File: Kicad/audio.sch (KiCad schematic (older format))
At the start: 71 parts, among them J601 Line Out, J602 AC'97 Audio Header, J603 CD Audio In, U601 TLV320AIC23BPW, U602 STX-4335-5BGP-S1, Y601 12M

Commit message: Switch some of the radial THT Electrolytic caps for SMD MLCCs.
Also changed the STM32 for an LQFP-32 as it has a bigger pitch on the
pins.

The LQFP is easier to solder than the TSSOP, and the MLCC takes are
cheaper and take up less space.
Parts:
- C601, C603, C611, C626, C633, C634, C635, C636, C637, C638: value 10u -> 10u 10V; footprint Capacitor_THT:CP_Radial_D6.3mm_P2.50mm -> Capacitor_SMD:C_0805_2012Metric_Pad1.15x1.40mm_HandSolder; symbol Device:CP -> Device:C; Digikey 493-10359-1-ND -> 1276-6455-1-ND; MPN UMW1E100MDD1TP -> CL21A106KOQNNNG; Manufacturer Nichicon -> Samsung
- C605, C606, C620, C621: symbol Device:CP_Small -> Device:C_Small
- C614, C615: value 220u -> 220u 16V
- C630: value 1u -> 1u 10V; footprint Capacitor_THT:CP_Radial_D6.3mm_P2.50mm -> Capacitor_SMD:C_0805_2012Metric_Pad1.15x1.40mm_HandSolder; symbol Device:CP_Small -> Device:C_Small; Digikey 493-10944-1-ND -> 1276-6471-1-ND; MPN UFG1H010MDM1TD -> CL21B105KOFNNNG; Manufacturer Nichicon -> Samsung
- FB601, FB602, FB603, FB604, FB605, FB606, FB608, FB609, FB610, FB611: value 220R@100MHz -> 3k3
- R601, R602: value 100 -> 100R
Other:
- moved on the sheet: C602, C607, C609, C610, C612, C613, C627, FB601, FB611

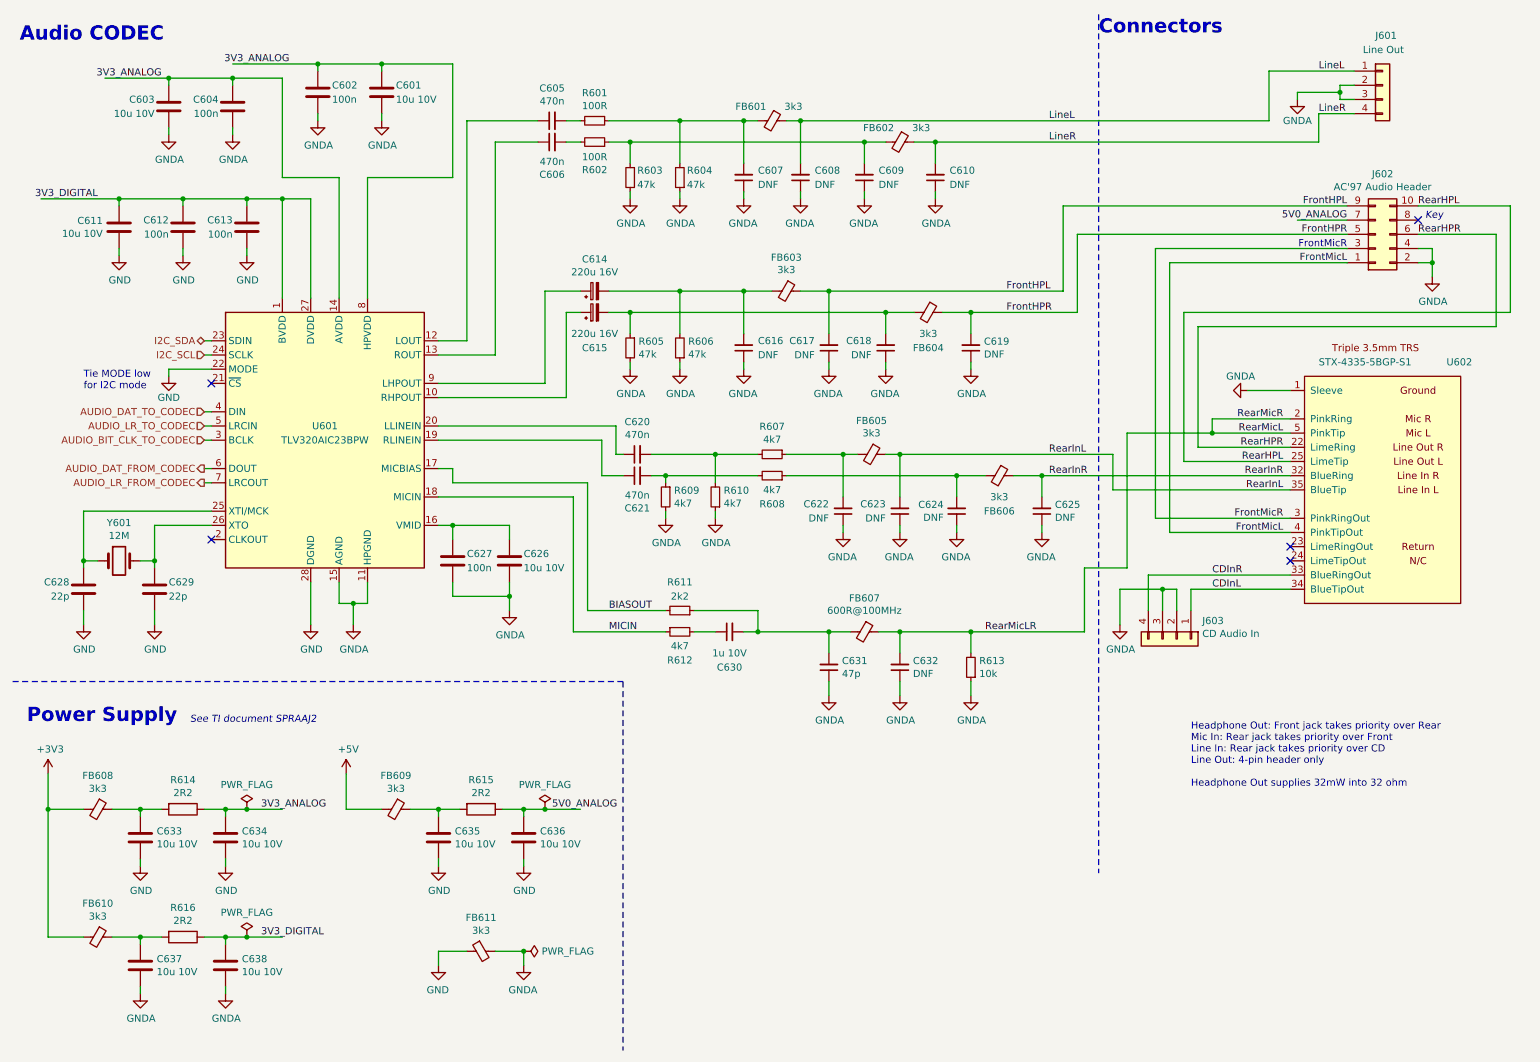
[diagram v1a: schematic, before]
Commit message: Added 12-bit video DAC.
Also had to change footprints to suit Kicad 5.1.9
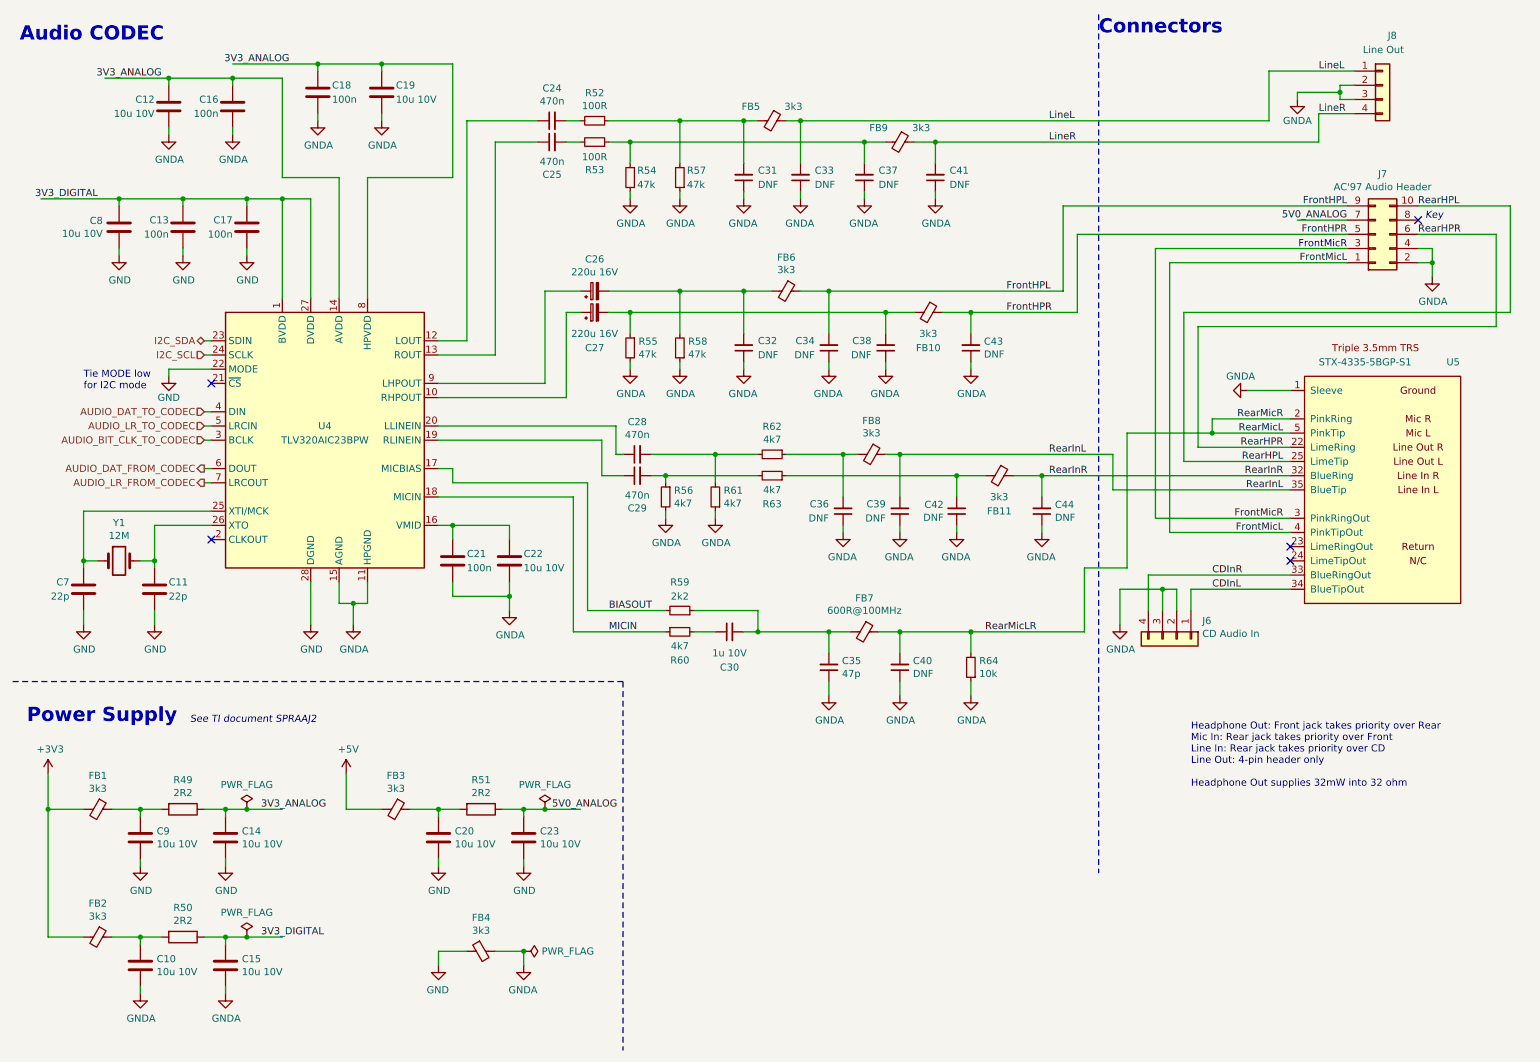
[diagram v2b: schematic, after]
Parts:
- C10: renamed from C637; footprint Capacitor_SMD:C_0805_2012Metric_Pad1.15x1.40mm_HandSolder -> Capacitor_SMD:C_0805_2012Metric_Pad1.18x1.45mm_HandSolder
- C11: renamed from C629; footprint Capacitor_SMD:C_0805_2012Metric_Pad1.15x1.40mm_HandSolder -> Capacitor_SMD:C_0805_2012Metric_Pad1.18x1.45mm_HandSolder
- C12: renamed from C603; footprint Capacitor_SMD:C_0805_2012Metric_Pad1.15x1.40mm_HandSolder -> Capacitor_SMD:C_0805_2012Metric_Pad1.18x1.45mm_HandSolder
- C13: renamed from C612; footprint Capacitor_SMD:C_0805_2012Metric_Pad1.15x1.40mm_HandSolder -> Capacitor_SMD:C_0805_2012Metric_Pad1.18x1.45mm_HandSolder
- C14: renamed from C634; footprint Capacitor_SMD:C_0805_2012Metric_Pad1.15x1.40mm_HandSolder -> Capacitor_SMD:C_0805_2012Metric_Pad1.18x1.45mm_HandSolder
- C15: renamed from C638; footprint Capacitor_SMD:C_0805_2012Metric_Pad1.15x1.40mm_HandSolder -> Capacitor_SMD:C_0805_2012Metric_Pad1.18x1.45mm_HandSolder
- C16: renamed from C604; footprint Capacitor_SMD:C_0805_2012Metric_Pad1.15x1.40mm_HandSolder -> Capacitor_SMD:C_0805_2012Metric_Pad1.18x1.45mm_HandSolder
- C17: renamed from C613; footprint Capacitor_SMD:C_0805_2012Metric_Pad1.15x1.40mm_HandSolder -> Capacitor_SMD:C_0805_2012Metric_Pad1.18x1.45mm_HandSolder
- C18: renamed from C602; footprint Capacitor_SMD:C_0805_2012Metric_Pad1.15x1.40mm_HandSolder -> Capacitor_SMD:C_0805_2012Metric_Pad1.18x1.45mm_HandSolder
- C19: renamed from C601; footprint Capacitor_SMD:C_0805_2012Metric_Pad1.15x1.40mm_HandSolder -> Capacitor_SMD:C_0805_2012Metric_Pad1.18x1.45mm_HandSolder
- C20: renamed from C635; footprint Capacitor_SMD:C_0805_2012Metric_Pad1.15x1.40mm_HandSolder -> Capacitor_SMD:C_0805_2012Metric_Pad1.18x1.45mm_HandSolder
- C21: renamed from C627; footprint Capacitor_SMD:C_0805_2012Metric_Pad1.15x1.40mm_HandSolder -> Capacitor_SMD:C_0805_2012Metric_Pad1.18x1.45mm_HandSolder
- C22: renamed from C626; footprint Capacitor_SMD:C_0805_2012Metric_Pad1.15x1.40mm_HandSolder -> Capacitor_SMD:C_0805_2012Metric_Pad1.18x1.45mm_HandSolder
- C23: renamed from C636; footprint Capacitor_SMD:C_0805_2012Metric_Pad1.15x1.40mm_HandSolder -> Capacitor_SMD:C_0805_2012Metric_Pad1.18x1.45mm_HandSolder
- C24: renamed from C605; footprint Capacitor_SMD:C_0805_2012Metric_Pad1.15x1.40mm_HandSolder -> Capacitor_SMD:C_0805_2012Metric_Pad1.18x1.45mm_HandSolder
- C25: renamed from C606; footprint Capacitor_SMD:C_0805_2012Metric_Pad1.15x1.40mm_HandSolder -> Capacitor_SMD:C_0805_2012Metric_Pad1.18x1.45mm_HandSolder
- C28: renamed from C620; footprint Capacitor_SMD:C_0805_2012Metric_Pad1.15x1.40mm_HandSolder -> Capacitor_SMD:C_0805_2012Metric_Pad1.18x1.45mm_HandSolder
- C29: renamed from C621; footprint Capacitor_SMD:C_0805_2012Metric_Pad1.15x1.40mm_HandSolder -> Capacitor_SMD:C_0805_2012Metric_Pad1.18x1.45mm_HandSolder
- C30: renamed from C630; footprint Capacitor_SMD:C_0805_2012Metric_Pad1.15x1.40mm_HandSolder -> Capacitor_SMD:C_0805_2012Metric_Pad1.18x1.45mm_HandSolder
- C31: renamed from C607; footprint Capacitor_SMD:C_0805_2012Metric_Pad1.15x1.40mm_HandSolder -> Capacitor_SMD:C_0805_2012Metric_Pad1.18x1.45mm_HandSolder
- C32: renamed from C616; footprint Capacitor_SMD:C_0805_2012Metric_Pad1.15x1.40mm_HandSolder -> Capacitor_SMD:C_0805_2012Metric_Pad1.18x1.45mm_HandSolder
- C33: renamed from C608; footprint Capacitor_SMD:C_0805_2012Metric_Pad1.15x1.40mm_HandSolder -> Capacitor_SMD:C_0805_2012Metric_Pad1.18x1.45mm_HandSolder
- C34: renamed from C617; footprint Capacitor_SMD:C_0805_2012Metric_Pad1.15x1.40mm_HandSolder -> Capacitor_SMD:C_0805_2012Metric_Pad1.18x1.45mm_HandSolder
- C35: renamed from C631; footprint Capacitor_SMD:C_0805_2012Metric_Pad1.15x1.40mm_HandSolder -> Capacitor_SMD:C_0805_2012Metric_Pad1.18x1.45mm_HandSolder
- C36: renamed from C622; footprint Capacitor_SMD:C_0805_2012Metric_Pad1.15x1.40mm_HandSolder -> Capacitor_SMD:C_0805_2012Metric_Pad1.18x1.45mm_HandSolder
- C37: renamed from C609; footprint Capacitor_SMD:C_0805_2012Metric_Pad1.15x1.40mm_HandSolder -> Capacitor_SMD:C_0805_2012Metric_Pad1.18x1.45mm_HandSolder
- C38: renamed from C618; footprint Capacitor_SMD:C_0805_2012Metric_Pad1.15x1.40mm_HandSolder -> Capacitor_SMD:C_0805_2012Metric_Pad1.18x1.45mm_HandSolder
- C39: renamed from C623; footprint Capacitor_SMD:C_0805_2012Metric_Pad1.15x1.40mm_HandSolder -> Capacitor_SMD:C_0805_2012Metric_Pad1.18x1.45mm_HandSolder
- C40: renamed from C632; footprint Capacitor_SMD:C_0805_2012Metric_Pad1.15x1.40mm_HandSolder -> Capacitor_SMD:C_0805_2012Metric_Pad1.18x1.45mm_HandSolder
- C41: renamed from C610; footprint Capacitor_SMD:C_0805_2012Metric_Pad1.15x1.40mm_HandSolder -> Capacitor_SMD:C_0805_2012Metric_Pad1.18x1.45mm_HandSolder
- C42: renamed from C624; footprint Capacitor_SMD:C_0805_2012Metric_Pad1.15x1.40mm_HandSolder -> Capacitor_SMD:C_0805_2012Metric_Pad1.18x1.45mm_HandSolder
- C43: renamed from C619; footprint Capacitor_SMD:C_0805_2012Metric_Pad1.15x1.40mm_HandSolder -> Capacitor_SMD:C_0805_2012Metric_Pad1.18x1.45mm_HandSolder
- C44: renamed from C625; footprint Capacitor_SMD:C_0805_2012Metric_Pad1.15x1.40mm_HandSolder -> Capacitor_SMD:C_0805_2012Metric_Pad1.18x1.45mm_HandSolder
- C7: renamed from C628; footprint Capacitor_SMD:C_0805_2012Metric_Pad1.15x1.40mm_HandSolder -> Capacitor_SMD:C_0805_2012Metric_Pad1.18x1.45mm_HandSolder
- C8: renamed from C611; footprint Capacitor_SMD:C_0805_2012Metric_Pad1.15x1.40mm_HandSolder -> Capacitor_SMD:C_0805_2012Metric_Pad1.18x1.45mm_HandSolder
- C9: renamed from C633; footprint Capacitor_SMD:C_0805_2012Metric_Pad1.15x1.40mm_HandSolder -> Capacitor_SMD:C_0805_2012Metric_Pad1.18x1.45mm_HandSolder
- R49: renamed from R614; footprint Resistor_SMD:R_0805_2012Metric_Pad1.15x1.40mm_HandSolder -> Resistor_SMD:R_0805_2012Metric_Pad1.20x1.40mm_HandSolder
- R50: renamed from R616; footprint Resistor_SMD:R_0805_2012Metric_Pad1.15x1.40mm_HandSolder -> Resistor_SMD:R_0805_2012Metric_Pad1.20x1.40mm_HandSolder
- R51: renamed from R615; footprint Resistor_SMD:R_0805_2012Metric_Pad1.15x1.40mm_HandSolder -> Resistor_SMD:R_0805_2012Metric_Pad1.20x1.40mm_HandSolder
- R52: renamed from R601; footprint Resistor_SMD:R_0805_2012Metric_Pad1.15x1.40mm_HandSolder -> Resistor_SMD:R_0805_2012Metric_Pad1.20x1.40mm_HandSolder
- R53: renamed from R602; footprint Resistor_SMD:R_0805_2012Metric_Pad1.15x1.40mm_HandSolder -> Resistor_SMD:R_0805_2012Metric_Pad1.20x1.40mm_HandSolder
- R54: renamed from R603; footprint Resistor_SMD:R_0805_2012Metric_Pad1.15x1.40mm_HandSolder -> Resistor_SMD:R_0805_2012Metric_Pad1.20x1.40mm_HandSolder
- R55: renamed from R605; footprint Resistor_SMD:R_0805_2012Metric_Pad1.15x1.40mm_HandSolder -> Resistor_SMD:R_0805_2012Metric_Pad1.20x1.40mm_HandSolder
- R56: renamed from R609; footprint Resistor_SMD:R_0805_2012Metric_Pad1.15x1.40mm_HandSolder -> Resistor_SMD:R_0805_2012Metric_Pad1.20x1.40mm_HandSolder
- R57: renamed from R604; footprint Resistor_SMD:R_0805_2012Metric_Pad1.15x1.40mm_HandSolder -> Resistor_SMD:R_0805_2012Metric_Pad1.20x1.40mm_HandSolder
- R58: renamed from R606; footprint Resistor_SMD:R_0805_2012Metric_Pad1.15x1.40mm_HandSolder -> Resistor_SMD:R_0805_2012Metric_Pad1.20x1.40mm_HandSolder
- R59: renamed from R611; footprint Resistor_SMD:R_0805_2012Metric_Pad1.15x1.40mm_HandSolder -> Resistor_SMD:R_0805_2012Metric_Pad1.20x1.40mm_HandSolder
- R60: renamed from R612; footprint Resistor_SMD:R_0805_2012Metric_Pad1.15x1.40mm_HandSolder -> Resistor_SMD:R_0805_2012Metric_Pad1.20x1.40mm_HandSolder
- R61: renamed from R610; footprint Resistor_SMD:R_0805_2012Metric_Pad1.15x1.40mm_HandSolder -> Resistor_SMD:R_0805_2012Metric_Pad1.20x1.40mm_HandSolder
- R62: renamed from R607; footprint Resistor_SMD:R_0805_2012Metric_Pad1.15x1.40mm_HandSolder -> Resistor_SMD:R_0805_2012Metric_Pad1.20x1.40mm_HandSolder
- R63: renamed from R608; footprint Resistor_SMD:R_0805_2012Metric_Pad1.15x1.40mm_HandSolder -> Resistor_SMD:R_0805_2012Metric_Pad1.20x1.40mm_HandSolder
- R64: renamed from R613; footprint Resistor_SMD:R_0805_2012Metric_Pad1.15x1.40mm_HandSolder -> Resistor_SMD:R_0805_2012Metric_Pad1.20x1.40mm_HandSolder
- renumbered C614 to C26, C615 to C27, FB608 to FB1, FB604 to FB10, FB606 to FB11, FB610 to FB2, FB609 to FB3, FB611 to FB4, FB601 to FB5, FB603 to FB6, FB607 to FB7, FB605 to FB8, FB602 to FB9, J603 to J6, J602 to J7, J601 to J8, U601 to U4, U602 to U5, Y601 to Y1

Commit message: Add 4-bit Video DAC, and re-wire BMC.
Now the BMC is an SPI device, and has a four-wire UART.
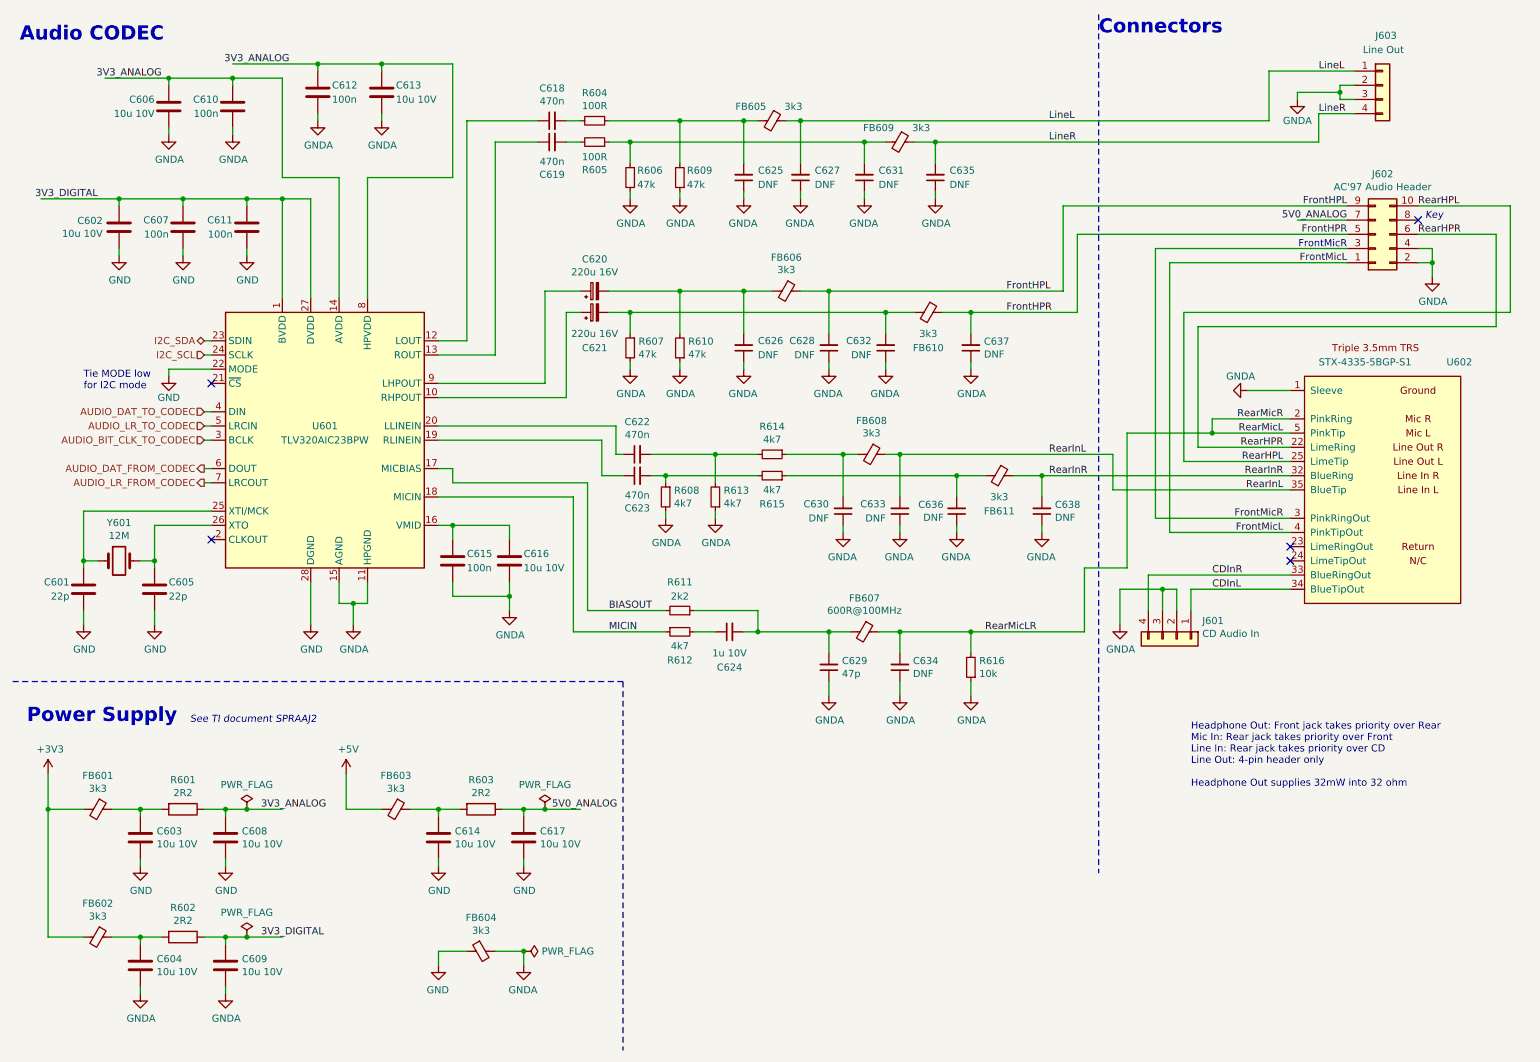
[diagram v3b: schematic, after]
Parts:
- renumbered C7 to C601, C8 to C602, C9 to C603, C10 to C604, C11 to C605, C12 to C606, C13 to C607, C14 to C608, C15 to C609, C16 to C610, C17 to C611, C18 to C612, C19 to C613, C20 to C614, C21 to C615, C22 to C616, C23 to C617, C24 to C618, C25 to C619, C26 to C620, C27 to C621, C28 to C622, C29 to C623, C30 to C624, C31 to C625, C32 to C626, C33 to C627, C34 to C628, C35 to C629, C36 to C630, C37 to C631, C38 to C632, C39 to C633, C40 to C634, C41 to C635, C42 to C636, C43 to C637, C44 to C638, FB1 to FB601, FB2 to FB602, FB3 to FB603, FB4 to FB604, FB5 to FB605, FB6 to FB606, FB7 to FB607, FB8 to FB608, FB9 to FB609, FB10 to FB610, FB11 to FB611, J6 to J601, J7 to J602, J8 to J603, R49 to R601, R50 to R602, R51 to R603, R52 to R604, R53 to R605, R54 to R606, R55 to R607, R56 to R608, R57 to R609, R58 to R610, R59 to R611, R60 to R612, R61 to R613, R62 to R614, R63 to R615, R64 to R616, U4 to U601, U5 to U602, Y1 to Y601

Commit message: Tidy up part nos and swapped I2C/UART on BMC.
Mark all resistors as 1% if not specified.
Added some Mouser part numbers.
BMC can now be programmed over UART.
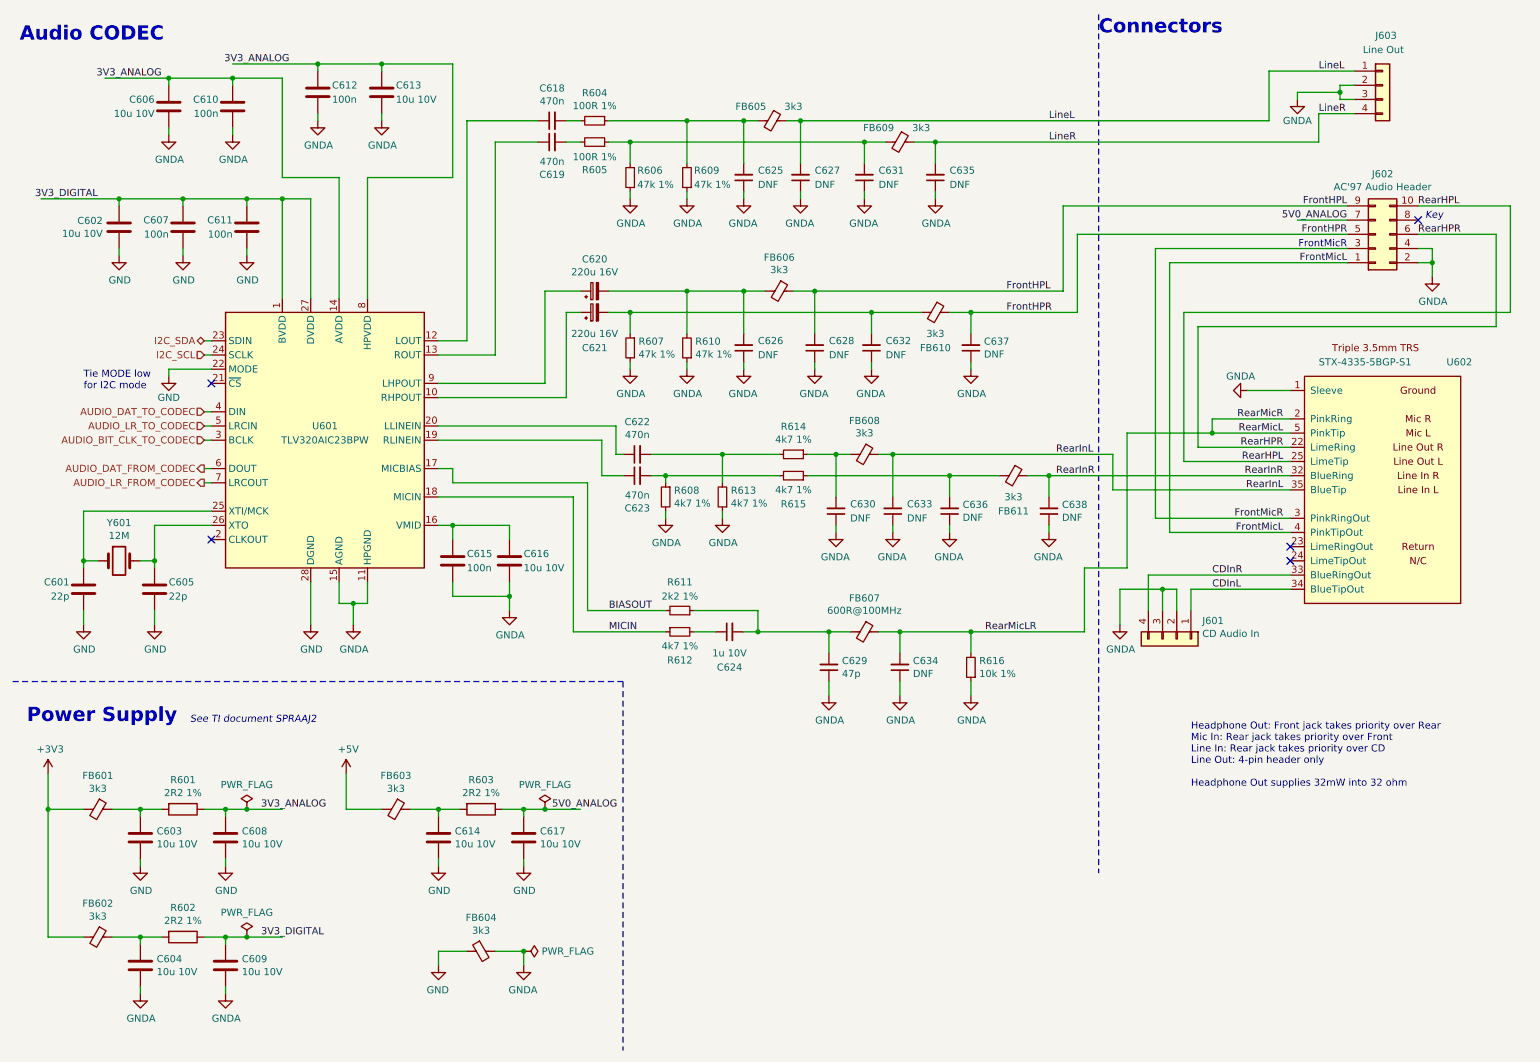
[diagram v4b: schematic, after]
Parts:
- C607, C610, C611, C612, C615: Mouser (none) -> 594-K104K15X7RF5TL2
- C618, C619, C622, C623: Mouser (none) -> 810-FG18X7R1H474KRT6
- C620, C621: Mouser (none) -> 647-UKT1C221MED
- FB601, FB602, FB603, FB604, FB605, FB606, FB608, FB609, FB610, FB611: Mouser (none) -> 81-BLM21P221SG
- FB607: Mouser (none) -> 875-HZ0805E601R-10
- R601, R602, R603: value 2R2 -> 2R2 1%
- R604, R605: value 100R -> 100R 1%
- R606, R607, R609, R610: value 47k -> 47k 1%; Digikey RMCF0805FG47K5-ND -> RMCF0805FT47K5-ND; MPN RMCF0805FG47K5 -> RMCF0805FT47K5
- R608, R612, R613, R614, R615: value 4k7 -> 4k7 1%
- R611: value 2k2 -> 2k2 1%
- R616: value 10k -> 10k 1%
- U601: Mouser (none) -> 595-TLV320AIC23BPW
- U602: Mouser (none) -> 806-STX-43355BGPS1
- Y601: Mouser (none) -> 815-ABL-12-B2
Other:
- moved on the sheet: C628, C630, C632, C633, C636, C638, FB606, FB608, FB610, FB611, R609, R610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
